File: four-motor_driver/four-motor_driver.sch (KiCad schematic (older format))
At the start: 47 parts, among them M1 MOTOR, M2 MOTOR, M3 MOTOR, M4 MOTOR

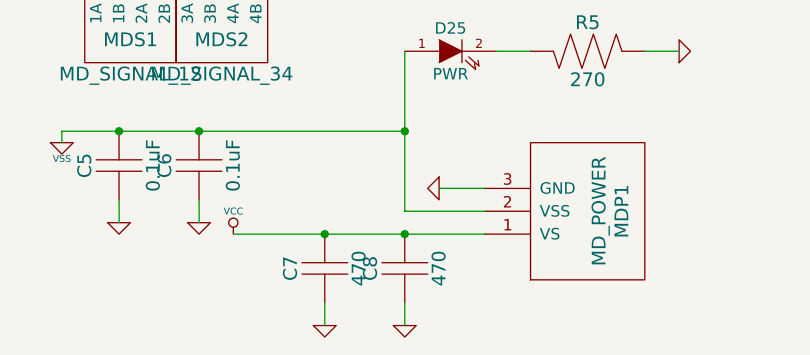
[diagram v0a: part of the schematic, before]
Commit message: Commit old changes that don't really matter anymore.
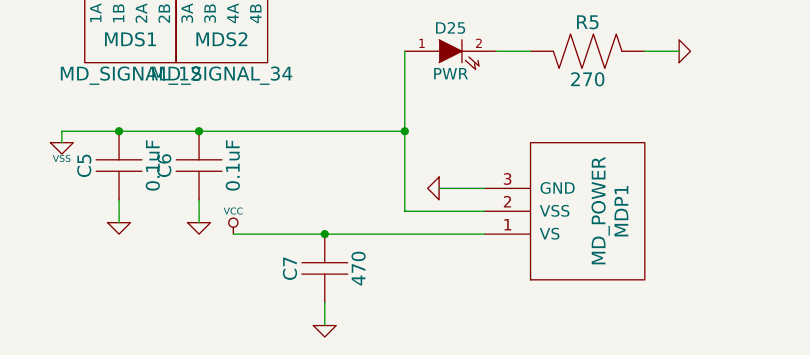
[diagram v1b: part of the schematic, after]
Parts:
- removed C8: 470, symbol CAP
